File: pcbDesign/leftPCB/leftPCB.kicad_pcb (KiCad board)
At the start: 4 copper layers, 57.5 x 90 mm, 17 parts, among them J1 Conn_01x12_Pin, SW1 UP, SW2 DOWN, SW3 LEFT, SW4 RIGHT

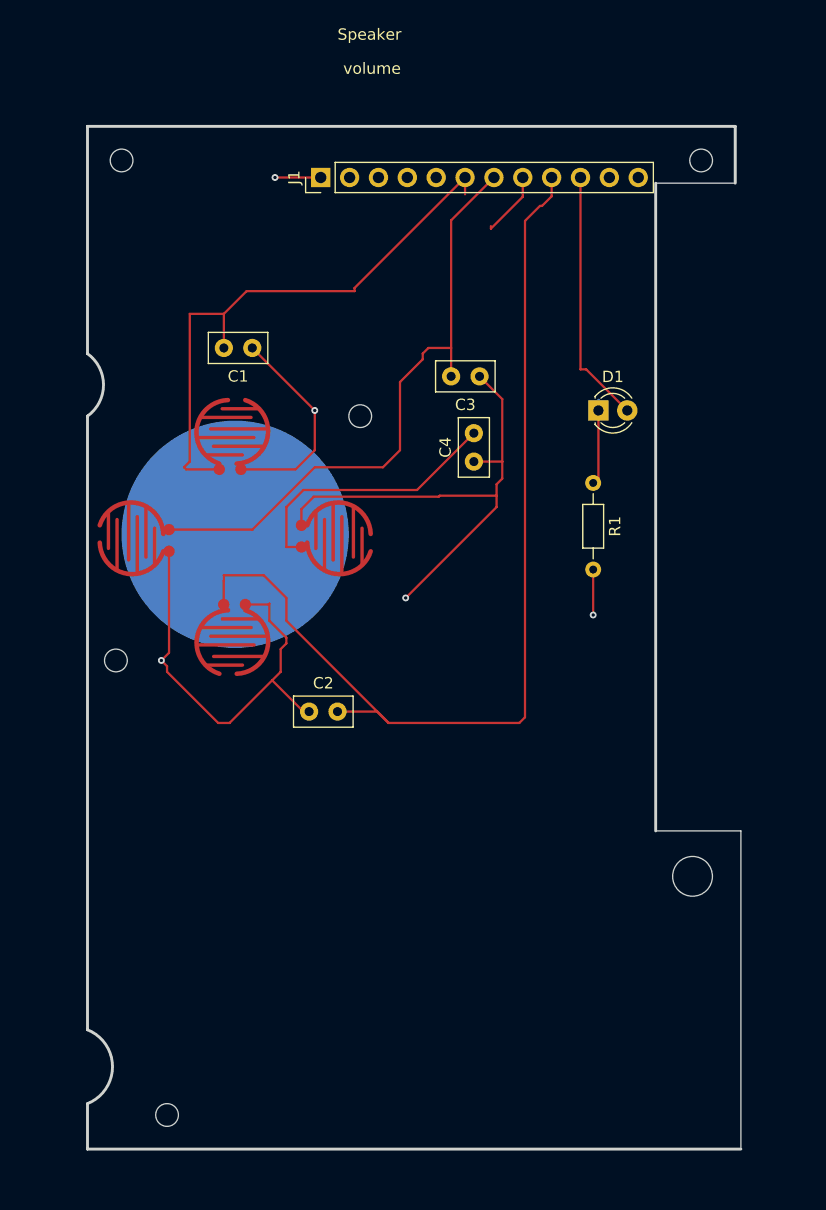
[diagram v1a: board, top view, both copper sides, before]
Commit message: Updated PCB designs for left and right boards
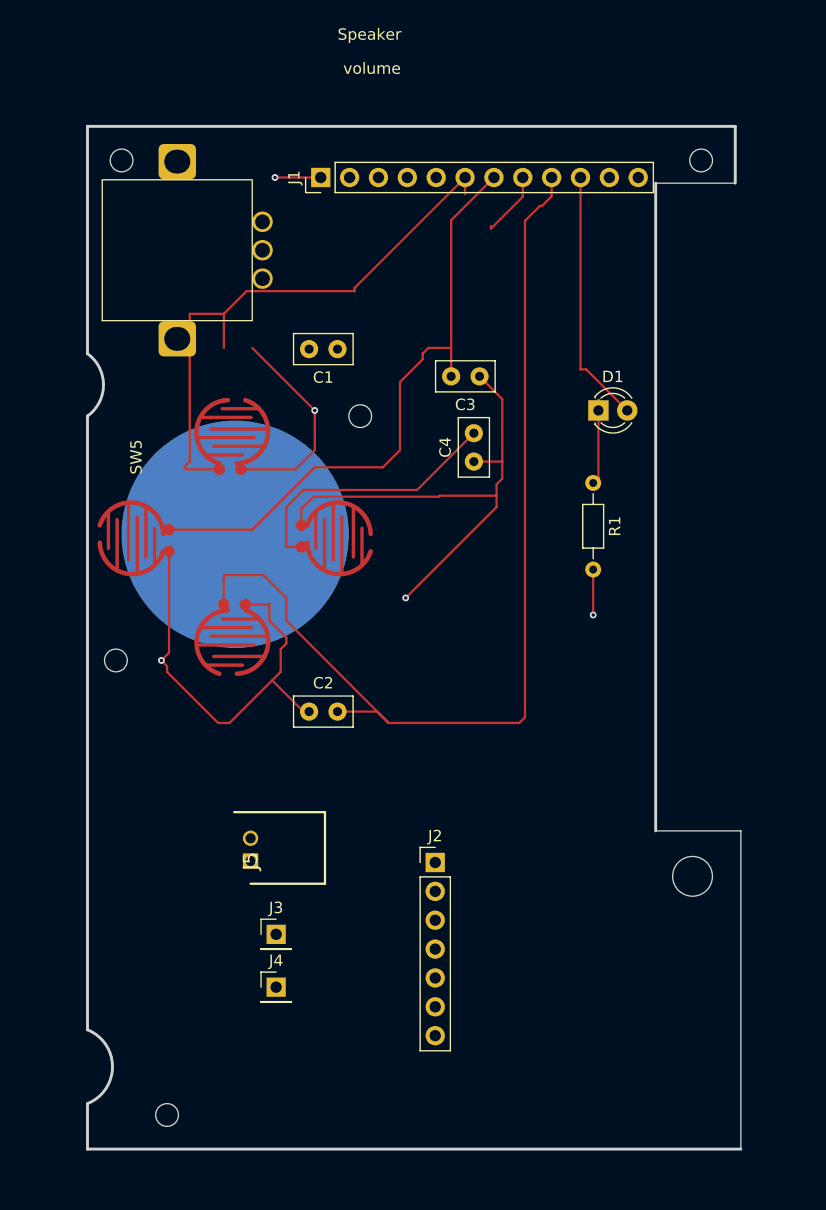
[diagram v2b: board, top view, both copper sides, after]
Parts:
- added J2: Conn_01x07_Pin, Connector_PinHeader_2.54mm:PinHeader_1x07_P2.54mm_Vertical, F.Cu at (152.6, 110.8)
- added J3: Conn_01x01_Pin, Connector_PinHeader_2.54mm:PinHeader_1x01_P2.54mm_Vertical, F.Cu at (138.6, 117.1)
- added J4: Conn_01x01_Pin, Connector_PinHeader_2.54mm:PinHeader_1x01_P2.54mm_Vertical, F.Cu at (138.6, 121.8)
- added J5: 440055-2, GGfoorptintLibrary:SHDRRA2W50P0X200_1X2_600X770X525P, F.Cu at (136.3, 110.7)
- added SW5: RotaryEncoder, GGfoorptintLibrary:PES12, F.Cu at (123.3, 63.1)
- moved C1 7.50 mm to (144.0, 65.6)
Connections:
- J1 pad 11: /3v3 -> /Clk
- J1 pad 2: /Clk -> /Volume_B
- J1 pad 4: /Volume_DT -> /Volume_A

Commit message: Routed
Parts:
- removed ? (x6): , 
- added H1: MountingHole, MountingHole:MountingHole_3.5mm, F.Cu at (175.2, 112.0)
- added H2: MountingHole, MountingHole:MountingHole_2mm, F.Cu at (129.0, 133.0)
- added H3: MountingHole, MountingHole:MountingHole_2mm, F.Cu at (124.5, 93.0)
- added H4: MountingHole, MountingHole:MountingHole_2mm, F.Cu at (146.0, 71.5)
- added H5: MountingHole, MountingHole:MountingHole_2mm, F.Cu at (125.0, 49.0)
- added H6: MountingHole, MountingHole:MountingHole_2mm, F.Cu at (176.0, 49.0)
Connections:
- SW2 pad 1: /Down -> GND
- SW2 pad 2: GND -> /Down
- SW3 pad 1: (no net) -> GND
- SW3 pad 2: (no net) -> /Left
- SW4 pad 1: (no net) -> GND
- SW4 pad 2: (no net) -> /Right
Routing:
- net /Clk: track 0.00 -> 83.1 mm
- net /5v: track 0.00 -> 78.5 mm, vias 0 -> 1
- net /LR_Clk: track 0.00 -> 77.7 mm
- net /D_In: track 0.00 -> 71.6 mm
- net GND: track 110.1 -> 166.0 mm, vias 5 -> 0
- net /Volume_A: track 0.00 -> 16.6 mm
- net /Right: track 29.9 -> 45.7 mm, vias 0 -> 1
- net /Speaker_Neg: track 0.00 -> 14.8 mm
- net /Down: track 89.3 -> 77.8 mm, vias 0 -> 2
- net /Volume_B: track 0.00 -> 11.3 mm
- net /Up: track 50.7 -> 42.7 mm
- net /Speaker_Pos: track 0.00 -> 7.38 mm
- net /Left: track 54.3 -> 50.5 mm, vias 0 -> 1
- net Net-(D1-K): track 7.75 -> 6.57 mm
- added copper zone on In1.Cu, net GND

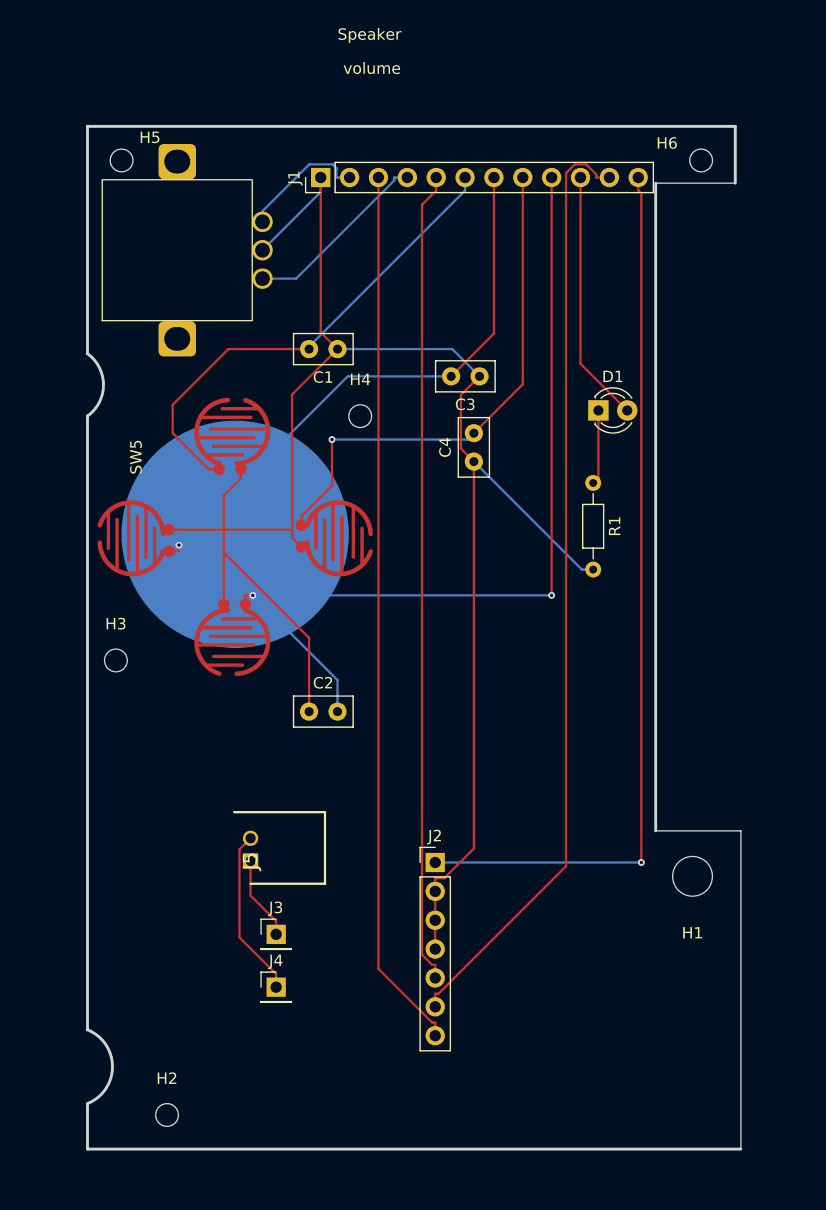
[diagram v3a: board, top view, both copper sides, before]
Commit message: Finalized placement on left pcb
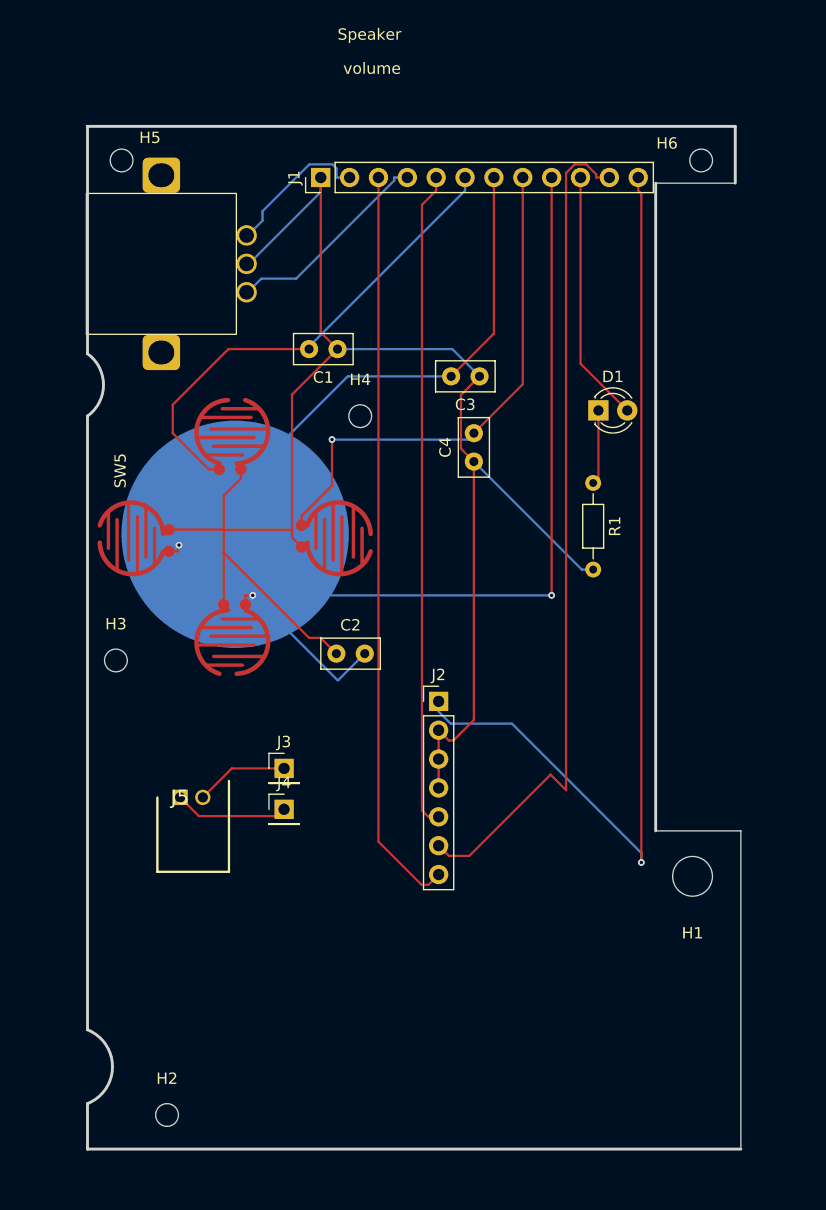
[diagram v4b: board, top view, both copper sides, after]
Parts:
- moved J4 15.7 mm to (139.3, 106.1)
- moved J3 14.6 mm to (139.3, 102.5)
- moved J2 14.2 mm to (152.9, 96.6)
- moved J5 8.35 mm to (130.2, 105.0), turned to 180 degrees
- moved C2 5.64 mm to (143.9, 92.4)
- moved SW5 1.84 mm to (121.9, 64.3)
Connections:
- J5 pad 1: /Speaker_Pos -> /Speaker_Neg
- J5 pad 2: /Speaker_Neg -> /Speaker_Pos
- SW2 pad 1: GND -> /Down
- SW2 pad 2: /Down -> GND
- SW3 pad 1: GND -> (no net)
- SW3 pad 2: /Left -> (no net)
- SW4 pad 1: GND -> (no net)
- SW4 pad 2: /Right -> (no net)
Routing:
- net GND: track 166.0 -> 151.6 mm
- net /D_In: track 71.6 -> 57.9 mm
- net /LR_Clk: track 77.7 -> 65.7 mm
- net /Clk: track 83.1 -> 74.2 mm
- net /5v: track 78.5 -> 85.1 mm
- net /Speaker_Neg: track 14.8 -> 10.1 mm
- net /Volume_A: track 16.6 -> 18.5 mm
- net /Volume_B: track 11.3 -> 13.1 mm
- net /Speaker_Pos: track 7.38 -> 8.21 mm
- net /Down: track 77.8 -> 78.4 mm

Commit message: Finalized center and left pcbs placemnt
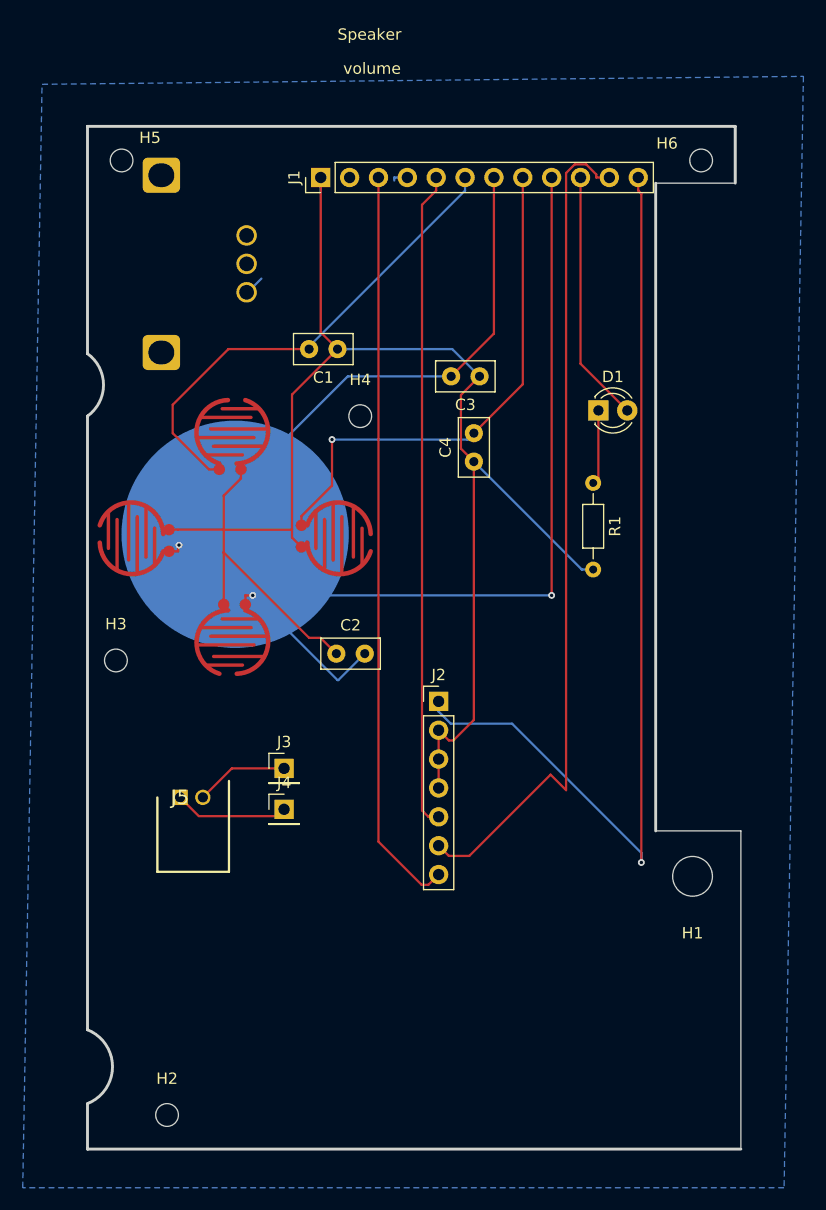
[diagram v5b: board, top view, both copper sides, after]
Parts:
- SW5: moved to B.Cu
- moved SW5 12.4 mm to (121.9, 51.9), turned to -90 degrees
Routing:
- net /Volume_A: track 18.5 -> 1.42 mm
- net /Volume_B: track 13.1 -> 1.80 mm
- net GND: track 151.6 -> 142.7 mm
- added copper zone on B.Cu, net GND
- removed copper zone on In1.Cu, net GND
- removed copper zone on In2.Cu, net GND
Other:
- copper layers 4 -> 2
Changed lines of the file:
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@@
 	(layers
 		(0 "F.Cu" signal)
-		(4 "In1.Cu" signal)
-		(6 "In2.Cu" signal)
 		(2 "B.Cu" signal)
 		(9 "F.Adhes" user "F.Adhesive")
@@
 			)
 			(layer "dielectric 1"
-				(type "prepreg")
-				(thickness 0.1)
-				(material "FR4")
-				(epsilon_r 4.5)
-				(loss_tangent 0.02)
-			)
-			(layer "In1.Cu"
-				(type "copper")
-				(thickness 0.035)
-			)
-			(layer "dielectric 2"
 				(type "core")
-				(thickness 1.24)
-				(material "FR4")
-				(epsilon_r 4.5)
-				(loss_tangent 0.02)
-			)
-			(layer "In2.Cu"
-				(type "copper")
-				(thickness 0.035)
-			)
-			(layer "dielectric 3"
-				(type "prepreg")
-				(thickness 0.1)
+				(thickness 1.51)
 				(material "FR4")
 				(epsilon_r 4.5)
@@
 		)
 	)
-	(footprint "GGfoorptintLibrary:PES12"
-		(layer "F.Cu")
-		(at 121.9 64.3 90)
-		(property "Reference" "SW5"
-			(at -12 3 90)
-			(unlocked yes)
-			(layer "F.SilkS")
-			(effects
-				(font
-					(size 1 1)
-					(thickness 0.1)
-				)
-			)
-		)
-		(property "Value" "RotaryEncoder"
-			(at 0 22 90)
-			(unlocked yes)
-			(layer "F.Fab")
-			(effects
-				(font
-					(size 1 1)
-					(thickness 0.15)
-				)
-			)
-		)
-		(property "Datasheet" ""
-			(at 0 0 90)
-			(unlocked yes)
-			(layer "F.Fab")
-			(hide yes)
-			(effects
-				(font
-					(size 1 1)
-					(thickness 0.15)
-				)
-			)
-		)
-		(property "Description" "Rotary encoder, dual channel, incremental quadrate outputs"
-			(at 0 0 90)
-			(unlocked yes)
-			(layer "F.Fab")
-			(hide yes)
-			(effects
-				(font
-					(size 1 1)
-					(thickness 0.15)
-				)
-			)
-		)
-		(property ki_fp_filters "RotaryEncoder*")
-		(sheetname "/")
-		(sheetfile "leftPCB.kicad_sch")
-		(attr smd)
-		(fp_rect
-			(start 0 0)
-			(end 12.4 13.2)
-			(stroke
-				(width 0.1)
-				(type solid)
-			)
-			(fill no)
-			(layer "F.SilkS")
-		)
-		(fp_text user "${REFERENCE}"
-			(at 0 24.5 90)
-			(unlocked yes)
-			(layer "F.Fab")
-			(effects
-				(font
-					(size 1 1)
-					(thickness 0.15)
-				)
-			)
-		)
-		(pad "" thru_hole roundrect
-			(at -1.6 6.6 90)
-			(size 3.1 3.3)
-			(drill oval 2.1 2.3)
-			(layers "*.Cu" "*.Mask")
-			(remove_unused_layers no)
-			(roundrect_rratio 0.15)
-			(thermal_bridge_angle 45)
-		)
-		(pad "" thru_hole roundrect
-			(at 14 6.6 90)
-			(size 3.1 3.3)
-			(drill oval 2.1 2.3)
-			(layers "*.Cu" "*.Mask")
-			(remove_unused_layers no)
-			(roundrect_rratio 0.15)
-			(thermal_bridge_angle 45)
-		)
-		(pad "A" thru_hole circle
-			(at 3.7 14.1 90)
-			(size 1.8 1.8)
-			(drill 1.3)
-			(layers "*.Cu" "*.Mask")
-			(remove_unused_layers no)
-			(net 1 "/Volume_A")
-			(pinfunction "A")
-			(pintype "passive")
-		)
-		(pad "B" thru_hole circle
-			(at 8.7 14.1 90)
-			(size 1.8 1.8)
-			(drill 1.3)
-			(layers "*.Cu" "*.Mask")
-			(remove_unused_layers no)
-			(net 5 "/Volume_B")
-			(pinfunction "B")
-			(pintype "passive")
-		)
-		(pad "C" thru_hole circle
-			(at 6.2 14.1 90)
-			(size 1.8 1.8)
-			(drill 1.3)
-			(layers "*.Cu" "*.Mask")
-			(remove_unused_layers no)
-			(net 8 "GND")
-			(pinfunction "C")
-			(pintype "passive")
-		)
-		(embedded_fonts no)
-	)
 	(footprint "Capacitor_THT:C_Disc_D5.0mm_W2.5mm_P2.50mm"
 		(layer "F.Cu")
@@
 		(embedded_fonts no)
 	)
+	(footprint "GGfoorptintLibrary:PES12"
+		(layer "B.Cu")
+		(at 121.9 51.9 -90)
+		(property "Reference" "SW5"
+			(at -12 -3 90)
+			(unlocked yes)
+			(layer "B.SilkS")
+			(effects
+				(font
+					(size 1 1)
+					(thickness 0.1)
+				)
+				(justify mirror)
+			)
+		)
+		(property "Value" "RotaryEncoder"
+			(at 0 -22 90)
+			(unlocked yes)
+			(layer "B.Fab")
+			(effects
+				(font
+					(size 1 1)
+					(thickness 0.15)
+				)
+				(justify mirror)
+			)
+		)
+		(property "Datasheet" ""
+			(at 0 0 90)
+			(unlocked yes)
+			(layer "B.Fab")
+			(hide yes)
+			(effects
+				(font
+					(size 1 1)
+					(thickness 0.15)
+				)
+				(justify mirror)
+			)
+		)
+		(property "Description" "Rotary encoder, dual channel, incremental quadrate outputs"
+			(at 0 0 90)
+			(unlocked yes)
+			(layer "B.Fab")
+			(hide yes)
+			(effects
+				(font
+					(size 1 1)
+					(thickness 0.15)
+				)
+				(justify mirror)
+			)
+		)
+		(property ki_fp_filters "RotaryEncoder*")
+		(sheetname "/")
+		(sheetfile "leftPCB.kicad_sch")
+		(attr smd)
+		(fp_rect
+			(start 0 0)
+			(end 12.4 -13.2)
+			(stroke
+				(width 0.1)
+				(type solid)
+			)
+			(fill no)
+			(layer "B.SilkS")
+		)
+		(fp_text user "${REFERENCE}"
+			(at 0 -24.5 90)
+			(unlocked yes)
+			(layer "B.Fab")
+			(effects
+				(font
+					(size 1 1)
+					(thickness 0.15)
+				)
+				(justify mirror)
+			)
+		)
+		(pad "" thru_hole roundrect
+			(at -1.6 -6.6 270)
+			(size 3.1 3.3)
+			(drill oval 2.1 2.3)
+			(layers "*.Cu" "*.Mask")
+			(remove_unused_layers no)
+			(roundrect_rratio 0.15)
+			(thermal_bridge_angle 45)
+		)
+		(pad "" thru_hole roundrect
+			(at 14 -6.6 270)
+			(size 3.1 3.3)
+			(drill oval 2.1 2.3)
+			(layers "*.Cu" "*.Mask")
+			(remove_unused_layers no)
+			(roundrect_rratio 0.15)
+			(thermal_bridge_angle 45)
+		)
+		(pad "A" thru_hole circle
+			(at 3.7 -14.1 270)
+			(size 1.8 1.8)
+			(drill 1.3)
+			(layers "*.Cu" "*.Mask")
+			(remove_unused_layers no)
+			(net 1 "/Volume_A")
+			(pinfunction "A")
+			(pintype "passive")
+		)
+		(pad "B" thru_hole circle
+			(at 8.7 -14.1 270)
+			(size 1.8 1.8)
+			(drill 1.3)
+			(layers "*.Cu" "*.Mask")
+			(remove_unused_layers no)
+			(net 5 "/Volume_B")
+			(pinfunction "B")
+			(pintype "passive")
+		)
+		(pad "C" thru_hole circle
+			(at 6.2 -14.1 270)
+			(size 1.8 1.8)
+			(drill 1.3)
+			(layers "*.Cu" "*.Mask")
+			(remove_unused_layers no)
+			(net 8 "GND")
+			(pinfunction "C")
+			(pintype "passive")
+		)
+		(embedded_fonts no)
+	)
 	(gr_circle
 		(center 134.994 81.898)
@@
 	)
 	(segment
-		(start 136 60.6)
-		(end 136.1 60.6)
-		(width 0.2)
-		(layer "B.Cu")
-		(net 1)
-	)
-	(segment
-		(start 136.1 60.6)
-		(end 137.3 59.4)
-		(width 0.2)
-		(layer "B.Cu")
-		(net 1)
-	)
-	(segment
 		(start 148.9933 50.5)
 		(end 150.145 50.5)
@@
 	)
 	(segment
-		(start 137.3 59.4)
-		(end 140.3618 59.4)
-		(width 0.2)
-		(layer "B.Cu")
-		(net 1)
-	)
-	(segment
-		(start 140.3618 59.4)
-		(end 148.9933 50.7685)
-		(width 0.2)
-		(layer "B.Cu")
-		(net 1)
-	)
-	(segment
 		(start 166.7733 50.5)
 		(end 167.925 50.5)
@@
 	)
 	(segment
-		(start 143.9133 50.5)
-		(end 145.065 50.5)
-		(width 0.2)
-		(layer "B.Cu")
-		(net 5)
-	)
-	(segment
-		(start 137.4 54.3)
-		(end 137.4 53.4687)
-		(width 0.2)
-		(layer "B.Cu")
-		(net 5)
-	)
-	(segment
-		(start 143.5761 49.3483)
-		(end 143.9133 49.6855)
-		(width 0.2)
-		(layer "B.Cu")
-		(net 5)
-	)
-	(segment
-		(start 143.9133 49.6855)
-		(end 143.9133 50.5)
-		(width 0.2)
-		(layer "B.Cu")
-		(net 5)
-	)
-	(segment
-		(start 136.1 55.6)
-		(end 137.4 54.3)
-		(width 0.2)
-		(layer "B.Cu")
-		(net 5)
-	)
-	(segment
-		(start 136 55.6)
-		(end 136.1 55.6)
-		(width 0.2)
-		(layer "B.Cu")
-		(net 5)
-	)
-	(segment
-		(start 141.5204 49.3483)
-		(end 143.5761 49.3483)
+		(start 136 60.6)
+		(end 136.1 60.6)
 		(width 0.2)
 		(layer "B.Cu")
@@
 	)
 	(segment
-		(start 137.4 53.4687)
-		(end 141.5204 49.3483)
+		(start 136.1 60.6)
+		(end 137.3 59.4)
 		(width 0.2)
 		(layer "B.Cu")
@@
 	)
 	(segment
-		(start 136.2 58.1)
-		(end 142.525 51.775)
-		(width 0.2)
-		(layer "B.Cu")
-		(net 8)
-	)
-	(segment
 		(start 142.525 51.775)
 		(end 142.525 50.5)
@@
 		(net 8)
 		(net_name "GND")
-		(layer "In1.Cu")
-		(hatch edge 0.5)
-		(connect_pads
-			(clearance 0.5)
-		)
-		(min_thickness 0.25)
-		(filled_areas_thickness no)
-		(fill yes
-			(thermal_gap 0.5)
-			(thermal_bridge_width 0.5)
-		)
-		(polygon
-			(pts
-				(xy 120.5 45) (xy 181 45) (xy 181 137) (xy 120.5 137)
-			)
-		)
-	)
-	(zone
-		(net 8)
-		(net_name "GND")
-		(layer "In2.Cu")
+		(layer "B.Cu")
 		(hatch edge 0.5)
-		(priority 1)
 		(connect_pads
 			(clearance 0.5)
@@
 		(polygon
 			(pts
-				(xy 120.5 45) (xy 181 45) (xy 181 137) (xy 120.5 137)
+				(xy 118 42.3) (xy 185 41.6) (xy 183.3 139.4) (xy 116.3 139.4)
 			)
 		)

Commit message: rerouted
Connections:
- SW2 pad 1: /Down -> GND
- SW2 pad 2: GND -> /Down
- SW3 pad 1: (no net) -> GND
- SW3 pad 2: (no net) -> /Left
- SW4 pad 1: (no net) -> GND
- SW4 pad 2: (no net) -> /Right
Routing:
- net /5v: track 85.1 -> 61.8 mm
- net /Volume_A: track 1.42 -> 17.8 mm
- net /Volume_B: track 1.80 -> 13.9 mm
- net GND: track 142.7 -> 131.6 mm
- net /Down: track 78.4 -> 69.7 mm, vias 2 -> 1
- net /Up: track 42.7 -> 36.0 mm, vias 0 -> 1
- net /Clk: track 74.2 -> 68.8 mm
- net /LR_Clk: track 65.7 -> 63.7 mm
